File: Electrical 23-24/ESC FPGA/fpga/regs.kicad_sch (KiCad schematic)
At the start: 0 parts

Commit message: Add fpga stuff and stencils
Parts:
- added C26, C33, C36, C43: 0.1u, symbol Device:C
- added C27, C28, C29, C31, C32, C37, C38, C39, C40, C41: 2.2u, symbol Device:C
- added C30, C42: 1u, symbol Device:C
- added C34, C44: 4.7n, symbol Device:C
- added C35, C45: 10u, symbol Device:C
- added D1 (x2): LED, symbol Device:LED
- added L1, L2: 3.9u, symbol Device:L
- added R15, R22: 1.42k, symbol Device:R
- added R16, R17, R23, R25: 2.2, symbol Device:R
- added R19, R20, R26, R27: 10k, symbol Device:R
- added R21, R28: 2.2k, symbol Device:R
- added R4 (x2): 470, symbol Device:R
- added U6, U7: MIC28515T-E/PHA, VQFN32_PHA_MCH, symbol fpga:MIC28515T-E_PHA
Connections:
- new net: D1.1 (K), R4.1 (x2)
- new net: R4.2, U7.32 (PG)
- new net: C43.1, R26.2
- new net: C40.2, R23.1, U7.21 (PVDD)
- new net: C30.2, R16.1, U6.31 (SVIN)
- new net: C42.2, R25.1, U7.31 (SVIN)
- new net: C36.2, U7.4 (BST)
- new net: C33.1, R19.2
- new net: R22.2, U7.1 (ILIM)
- new net: C26.2, U6.4 (BST)
- new net: R15.2, U6.1 (ILIM)
- new net: C31.2, R17.1, U6.21 (PVDD)
- new net: R4.2, U6.32 (PG)
- new net FB1: C33.2, C34.2, R20.2, R21.1, U6.27 (FB)
- new net FB2: C43.2, C44.2, R27.2, R28.1, U7.27 (FB)
- new net GND: C27.1, C28.1, C29.1, C30.1, C31.1, C32.1, C35.2, C37.1, C38.1, C39.1, C40.1, C41.1, C42.1, C45.2, R21.2, R28.2, U6.16 (PGND), U6.17 (PGND), U6.18 (PGND), U6.19 (PGND), U6.2 (PGND), U6.22 (PGND), U6.23 (EXTVDD), U6.26 (MODE), U6.28 (AGND), U6.29 (PGND), U6.33 (PGND), U7.16 (PGND), U7.17 (PGND), U7.18 (PGND), U7.19 (PGND), U7.2 (PGND), U7.22 (PGND), U7.23 (EXTVDD), U7.26 (MODE), U7.28 (AGND), U7.29 (PGND), U7.33 (PGND)
- new net SW1: C26.1, L1.1, R15.1, R19.1, U6.12 (SW), U6.13 (SW), U6.14 (SW), U6.15 (SW), U6.20 (SW), U6.3 (SW)
- new net SW2: C36.1, L2.1, R22.1, R26.1, U7.12 (SW), U7.13 (SW), U7.14 (SW), U7.15 (SW), U7.20 (SW), U7.3 (SW)
- new net VCCO_0: C34.1, C35.1, L1.2, R20.1
- new net VCC_INT: C44.1, C45.1, L2.2, R27.1
- new net VDD1: C32.2, D1.2 (A), R17.2, U6.30 (VDD)
- new net VDD2: C41.2, D1.2 (A), R23.2, U7.30 (VDD)
- new net VIN: C27.2, C28.2, C29.2, C37.2, C38.2, C39.2, R16.2, R25.2, U6.10 (VIN), U6.11 (VIN), U6.24 (EN), U6.25 (FREQ), U6.5 (VIN), U6.6 (VIN), U6.7 (VIN), U6.8 (VIN), U6.9 (VIN), U7.10 (VIN), U7.11 (VIN), U7.24 (EN), U7.25 (FREQ), U7.5 (VIN), U7.6 (VIN), U7.7 (VIN), U7.8 (VIN), U7.9 (VIN)
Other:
- note added: "10829"
- note added: "1V2"
- note added: "3V3"
- note added: "5V VDD 1.7V VF 8mA"
- note added: "need to choose power modes (diode connected?): -usb -power pin"

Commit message: Working on FPGA board
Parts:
- added C46, C49: 22n, symbol Device:C
- added C47, C51: 47u, symbol Device:C
- added C48, C50: 0.1u, symbol Device:C
- added J3: USB_B_Micro, Connector_USB:USB_Micro-B_Amphenol_10118193-0001LF_Horizontal, symbol Connector:USB_B_Micro
- added U10, U11: ~, Package_TO_SOT_SMD:LFPAK56, symbol fpga:NVMYS4D1N06CLTWG
- added U8, U9: LM74700QDBVRQ1, DBV0006A_N, symbol fpga:LM74700QDBVRQ1
- added XT60M1: XT60M, Connector_AMASS:AMASS_XT60IPW-M_1x03_P7.20mm_Horizontal, symbol PMB:XT60M
- C35, C45: value 10u -> 47u
- L2: value 3.9u -> 1.5u
- R26: value 10k -> 7.5k
- R28: value 2.2k -> 10k
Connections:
- net GND: now also C46.2, C47.2, C49.2, C51.2, J3.5 (GND), U8.2 (GND), U9.2 (GND), XT60M1.1 (-)
- net VIN: now also C47.1, C51.1, U10.5 (D), U11.5 (D), U8.4 (CATHODE), U9.4 (CATHODE)
- net VCCO_0 renamed 3V3
- new net: C48.2, U8.1 (VCAP)
- new net: U10.4 (G), U8.5 (GATE)
- new net: C50.2, U9.1 (VCAP)
- new net: U11.4 (G), U9.5 (GATE)
- new net VBATT: C48.1, C49.1, U10.1 (S), U10.2 (S), U10.3 (S), U8.3 (EN), U8.6 (ANODE), XT60M1.2 (+)
- new net VUSB: C46.1, C50.1, J3.1 (VBUS), U11.1 (S), U11.2 (S), U11.3 (S), U9.3 (EN), U9.6 (ANODE)
- no-connect marks 0 -> 4
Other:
- note added: "5V"
- note added: "7633"
- note added: "XXX"
- moved on the sheet: C26, C27, C28, C29, C30, C31, C32, C33, C34, C35, C36, C37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

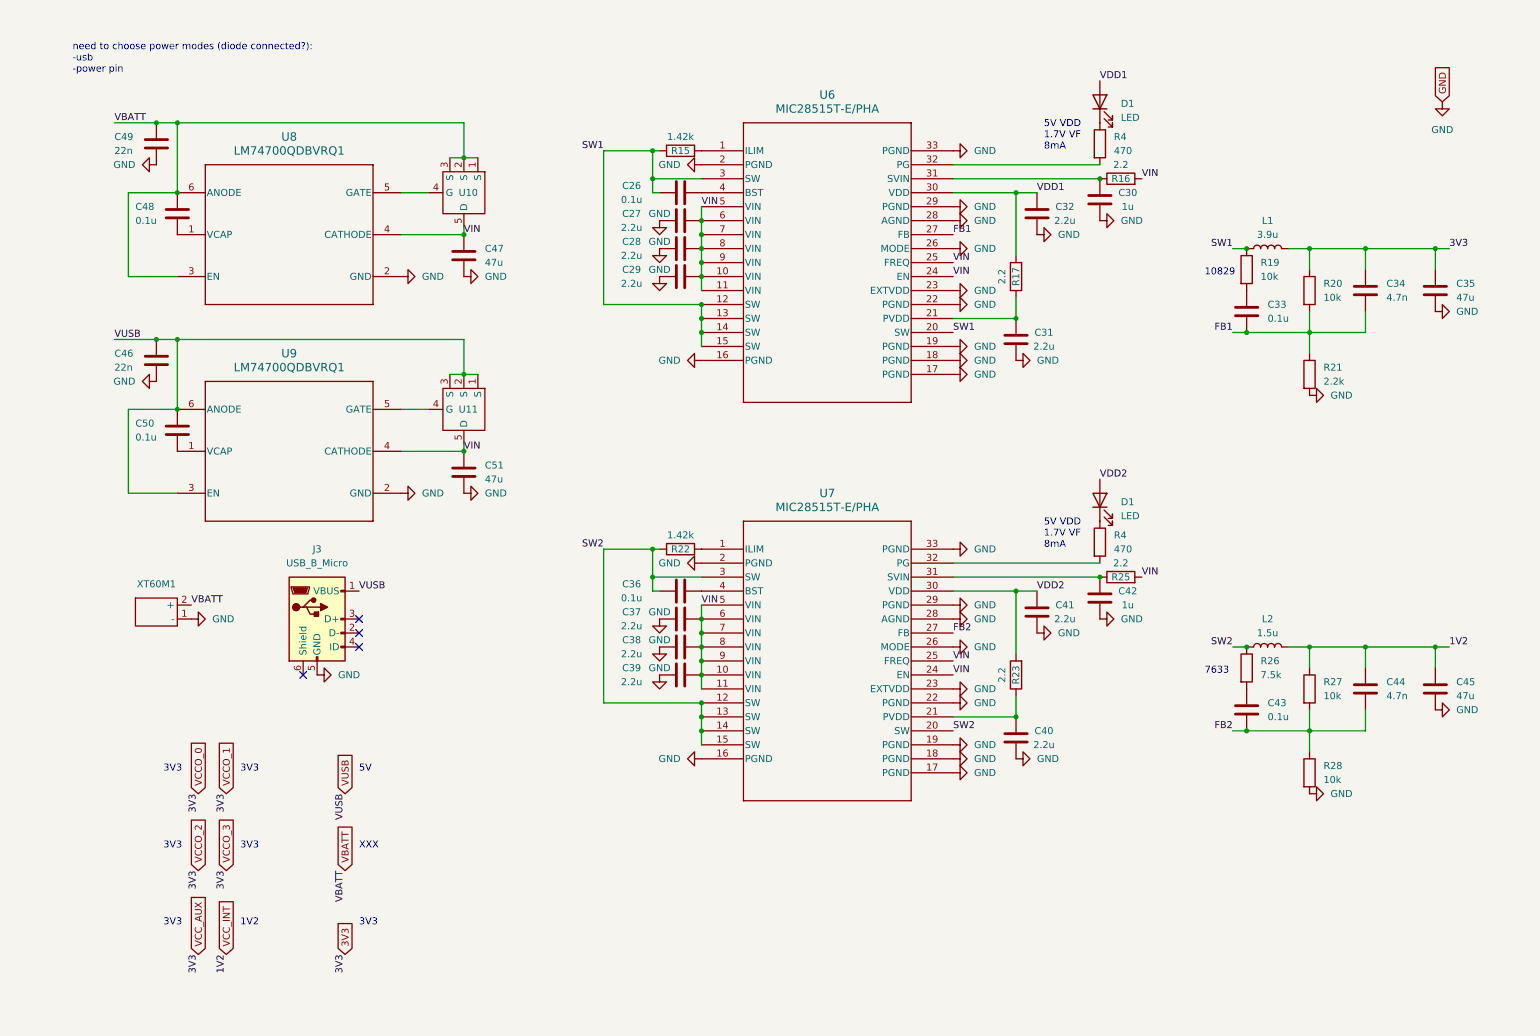
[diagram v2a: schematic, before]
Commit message: Add level shifters
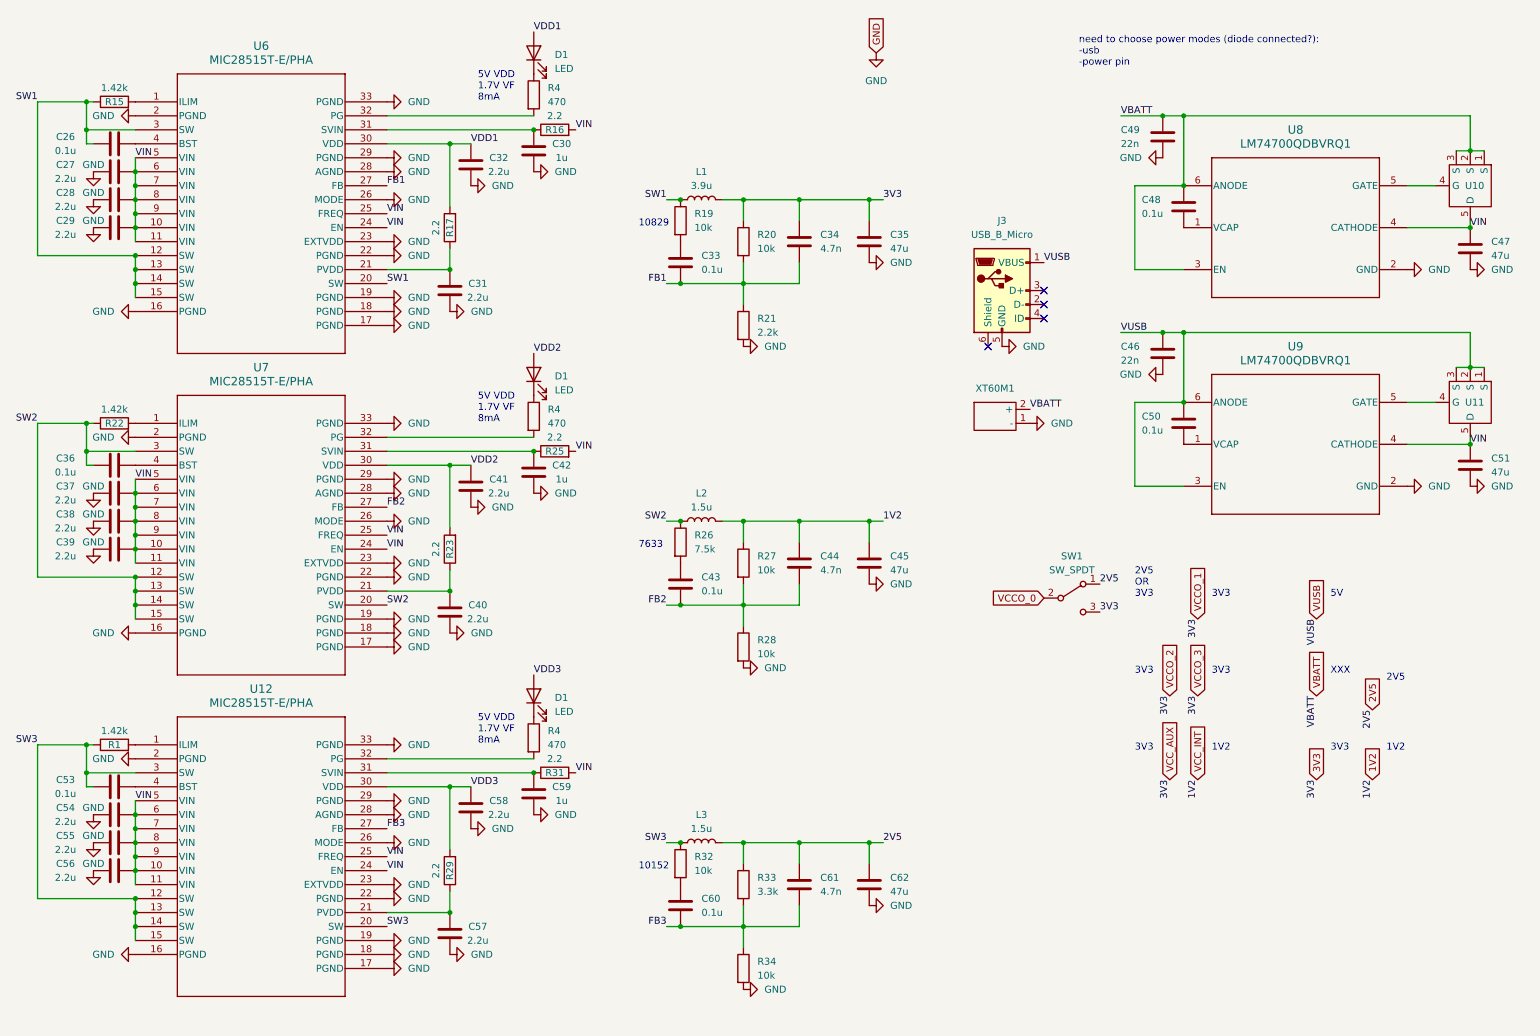
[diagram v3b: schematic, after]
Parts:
- added C53, C60: 0.1u, symbol Device:C
- added C54, C55, C56, C57, C58: 2.2u, symbol Device:C
- added C59: 1u, symbol Device:C
- added C61: 4.7n, symbol Device:C
- added C62: 47u, symbol Device:C
- added D1: LED, symbol Device:LED
- added L3: 1.5u, symbol Device:L
- added R1: 1.42k, symbol Device:R
- added R29, R31: 2.2, symbol Device:R
- added R32, R34: 10k, symbol Device:R
- added R33: 3.3k, symbol Device:R
- added R4: 470, symbol Device:R
- added SW1: SW_SPDT, symbol Switch:SW_SPDT
- added U12: MIC28515T-E/PHA, VQFN32_PHA_MCH, symbol fpga:MIC28515T-E_PHA
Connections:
- net 3V3: now also SW1.3 (C)
- net GND: now also C54.1, C55.1, C56.1, C57.1, C58.1, C59.1, C62.2, R34.2, U12.16 (PGND), U12.17 (PGND), U12.18 (PGND), U12.19 (PGND), U12.2 (PGND), U12.22 (PGND), U12.23 (EXTVDD), U12.26 (MODE), U12.28 (AGND), U12.29 (PGND), U12.33 (PGND)
- net VIN: now also C54.2, C55.2, C56.2, R31.2, U12.10 (VIN), U12.11 (VIN), U12.24 (EN), U12.25 (FREQ), U12.5 (VIN), U12.6 (VIN), U12.7 (VIN), U12.8 (VIN), U12.9 (VIN)
- net VCC_INT renamed 1V2
- new net: C60.1, R32.2
- new net: R1.2, U12.1 (ILIM)
- new net: D1.1 (K), R4.1
- new net: R4.2, U12.32 (PG)
- new net: C59.2, R31.1, U12.31 (SVIN)
- new net: C57.2, R29.1, U12.21 (PVDD)
- new net: C53.2, U12.4 (BST)
- new net 2V5: C61.1, C62.1, L3.2, R33.1, SW1.1 (A)
- new net FB3: C60.2, C61.2, R33.2, R34.1, U12.27 (FB)
- new net SW3: C53.1, L3.1, R1.1, R32.1, U12.12 (SW), U12.13 (SW), U12.14 (SW), U12.15 (SW), U12.20 (SW), U12.3 (SW)
- new net VCCO_0: SW1.2 (B)
- new net VDD3: C58.2, D1.2 (A), R29.2, U12.30 (VDD)
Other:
- note added: "10152"
- note added: "2V5"
- note added: "2V5 OR 3V3"
- moved on the sheet: C26, C27, C28, C29, C30, C31, C32, C33, C34, C35, C36, C37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

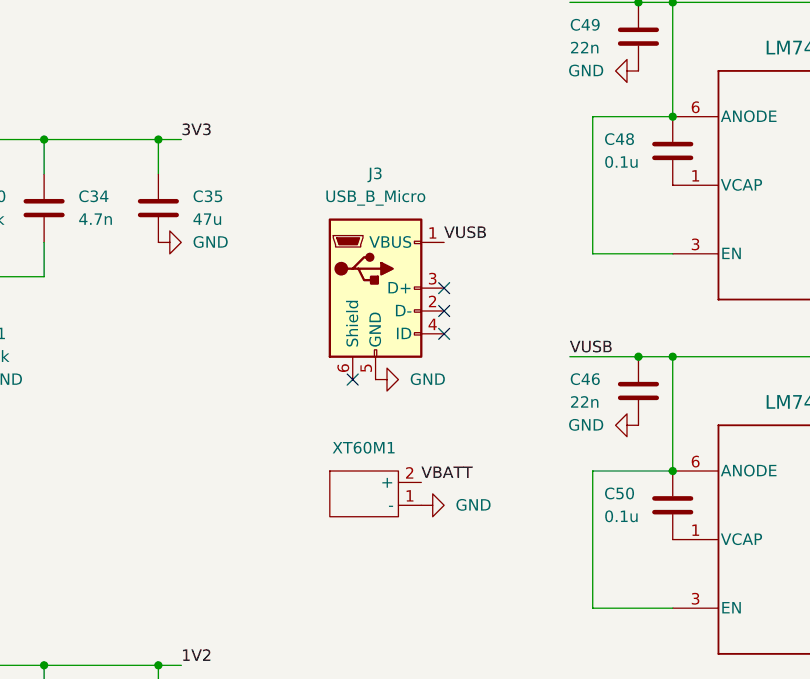
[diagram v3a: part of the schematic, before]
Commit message: Finished FPGA board schematic
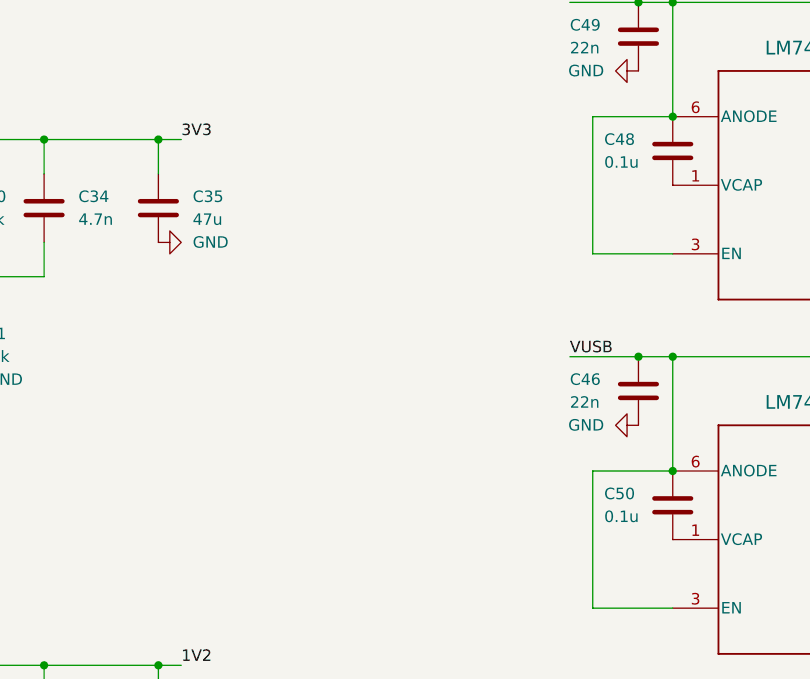
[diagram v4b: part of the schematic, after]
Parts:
- removed J3: USB_B_Micro, Connector_USB:USB_Micro-B_Amphenol_10118193-0001LF_Horizontal, symbol Connector:USB_B_Micro
- removed XT60M1: XT60M, Connector_AMASS:AMASS_XT60IPW-M_1x03_P7.20mm_Horizontal, symbol PMB:XT60M
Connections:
- no-connect marks 4 -> 0
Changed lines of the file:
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@@
   (junction (at 34.29 160.02) (diameter 0) (color 0 0 0 0)
   )
-  (no_connect (at 199.39 64.77))
-  (no_connect (at 199.39 62.23))
-  (no_connect (at 189.23 72.39))
-  (no_connect (at 199.39 67.31))
   (wire (pts (xy 34.29 154.94) (xy 34.29 157.48))
     (stroke (width 0) (type default))
@@
     (effects (font (size 1.27 1.27)) (justify left bottom))
   )
-  (label "VBATT" (at 196.85 83.82 0) (fields_autoplaced)
-    (effects (font (size 1.27 1.27)) (justify left bottom))
-  )
   (label "1V2" (at 259.08 151.13 270) (fields_autoplaced)
     (effects (font (size 1.27 1.27)) (justify right bottom))
@@
     (effects (font (size 1.27 1.27)) (justify right bottom))
   )
-  (label "VUSB" (at 199.39 57.15 0) (fields_autoplaced)
-    (effects (font (size 1.27 1.27)) (justify left bottom))
-  )
   (label "SW2" (at 130.81 104.14 180) (fields_autoplaced)
     (effects (font (size 1.27 1.27)) (justify right bottom))
@@
     )
   )
-  (symbol (lib_id "PMB:XT60M") (at 190.5 85.09 0) (unit 1)
-    (in_bom yes) (on_board yes) (dnp no) (fields_autoplaced)
-    (property "Reference" "XT60M1" (at 190.5 80.01 0)
-      (effects (font (size 1.27 1.27)))
-    )
-    (property "Value" "XT60M" (at 190.5 85.09 0)
-      (effects (font (size 1.27 1.27)) hide)
-    )
-    (property "Footprint" "Connector_AMASS:AMASS_XT60IPW-M_1x03_P7.20mm_Horizontal" (at 190.5 85.09 0)
-      (effects (font (size 1.27 1.27)) hide)
-    )
-    (property "Datasheet" "" (at 190.5 85.09 0)
-      (effects (font (size 1.27 1.27)) hide)
-    )
-    (pin "1")
-    (pin "2")
-    (instances
-      (project "fpga"
-        (path "/5bf59577-a814-4364-8f7a-37815cfb5474/a7f1449c-b9d7-4bec-9483-b96d0a6d3b19"
-          (reference "XT60M1") (unit 1)
-        )
-      )
-    )
-  )
   (symbol (lib_id "power:GND") (at 26.67 99.06 0) (unit 1)
     (in_bom yes) (on_board yes) (dnp no)
@@
     )
   )
-  (symbol (lib_id "power:GND") (at 191.77 72.39 90) (unit 1)
-    (in_bom yes) (on_board yes) (dnp no) (fields_autoplaced)
-    (property "Reference" "#PWR016" (at 198.12 72.39 0)
-      (effects (font (size 1.27 1.27)) hide)
-    )
-    (property "Value" "GND" (at 195.58 72.39 90)
-      (effects (font (size 1.27 1.27)) (justify right))
-    )
-    (property "Footprint" "" (at 191.77 72.39 0)
-      (effects (font (size 1.27 1.27)) hide)
-    )
-    (property "Datasheet" "" (at 191.77 72.39 0)
-      (effects (font (size 1.27 1.27)) hide)
-    )
-    (pin "1")
-    (instances
-      (project "fpga"
-        (path "/5bf59577-a814-4364-8f7a-37815cfb5474/3e04db34-3f8a-4742-be82-6fa24c009343"
-          (reference "#PWR016") (unit 1)
-        )
-        (path "/5bf59577-a814-4364-8f7a-37815cfb5474/1f83b38b-56ef-4110-879b-13379f9dd920"
-          (reference "#PWR026") (unit 1)
-        )
-        (path "/5bf59577-a814-4364-8f7a-37815cfb5474/a286b274-4434-47ab-983d-e64806fdcbd6"
-          (reference "#PWR036") (unit 1)
-        )
-        (path "/5bf59577-a814-4364-8f7a-37815cfb5474/a7f1449c-b9d7-4bec-9483-b96d0a6d3b19"
-          (reference "#PWR088") (unit 1)
-        )
-      )
-    )
-  )
   (symbol (lib_id "Device:C") (at 30.48 167.64 90) (unit 1)
     (in_bom yes) (on_board yes) (dnp no)
@@
     )
   )
-  (symbol (lib_id "power:GND") (at 196.85 86.36 90) (unit 1)
-    (in_bom yes) (on_board yes) (dnp no) (fields_autoplaced)
-    (property "Reference" "#PWR016" (at 203.2 86.36 0)
-      (effects (font (size 1.27 1.27)) hide)
-    )
-    (property "Value" "GND" (at 200.66 86.36 90)
-      (effects (font (size 1.27 1.27)) (justify right))
-    )
-    (property "Footprint" "" (at 196.85 86.36 0)
-      (effects (font (size 1.27 1.27)) hide)
-    )
-    (property "Datasheet" "" (at 196.85 86.36 0)
-      (effects (font (size 1.27 1.27)) hide)
-    )
-    (pin "1")
-    (instances
-      (project "fpga"
-        (path "/5bf59577-a814-4364-8f7a-37815cfb5474/3e04db34-3f8a-4742-be82-6fa24c009343"
-          (reference "#PWR016") (unit 1)
-        )
-        (path "/5bf59577-a814-4364-8f7a-37815cfb5474/1f83b38b-56ef-4110-879b-13379f9dd920"
-          (reference "#PWR026") (unit 1)
-        )
-        (path "/5bf59577-a814-4364-8f7a-37815cfb5474/a286b274-4434-47ab-983d-e64806fdcbd6"
-          (reference "#PWR036") (unit 1)
-        )
-        (path "/5bf59577-a814-4364-8f7a-37815cfb5474/a7f1449c-b9d7-4bec-9483-b96d0a6d3b19"
-          (reference "#PWR087") (unit 1)
-        )
-      )
-    )
-  )
   (symbol (lib_id "power:GND") (at 80.01 86.36 90) (unit 1)
     (in_bom yes) (on_board yes) (dnp no) (fields_autoplaced)
@@
         )
       )
-    )
-  )
-  (symbol (lib_id "Connector:USB_B_Micro") (at 191.77 62.23 0) (unit 1)
-    (in_bom yes) (on_board yes) (dnp no) (fields_autoplaced)
-    (property "Reference" "J3" (at 191.77 49.53 0)
-      (effects (font (size 1.27 1.27)))
-    )
-    (property "Value" "USB_B_Micro" (at 191.77 52.07 0)
-      (effects (font (size 1.27 1.27)))
-    )
-    (property "Footprint" "Connector_USB:USB_Micro-B_Amphenol_10118193-0001LF_Horizontal" (at 195.58 63.5 0)
-      (effects (font (size 1.27 1.27)) hide)
-    )
-    (property "Datasheet" "https://cdn.amphenol-cs.com/media/wysiwyg/files/documentation/datasheet/inputoutput/io_usb_micro.pdf" (at 195.58 63.5 0)
-      (effects (font (size 1.27 1.27)) hide)
-    )
-    (property "Digi" "https://www.digikey.com/en/products/detail/amphenol-cs-fci/10118193-0001LF/2785388" (at 191.77 62.23 0)
-      (effects (font (size 1.27 1.27)) hide)
-    )
-    (pin "1")
-    (pin "2")
-    (pin "3")
-    (pin "4")
-    (pin "5")
-    (pin "6")
-    (instances
-      (project "fpga"
-        (path "/5bf59577-a814-4364-8f7a-37815cfb5474/a7f1449c-b9d7-4bec-9483-b96d0a6d3b19"
-          (reference "J3") (unit 1)
-        )
-      )
-      (project "programmer"
-        (path "/aaaf4408-e4eb-45ee-a27d-c2b42f2a1569/1155aff1-def4-4854-ae66-7f7d5ef155d7"
-          (reference "J1") (unit 1)
-        )
-      )
